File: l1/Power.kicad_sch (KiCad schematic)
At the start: 31 parts, among them IC1 LM2587S-ADJ, U1 TPS5430DDA, U2 TPS5430DDA

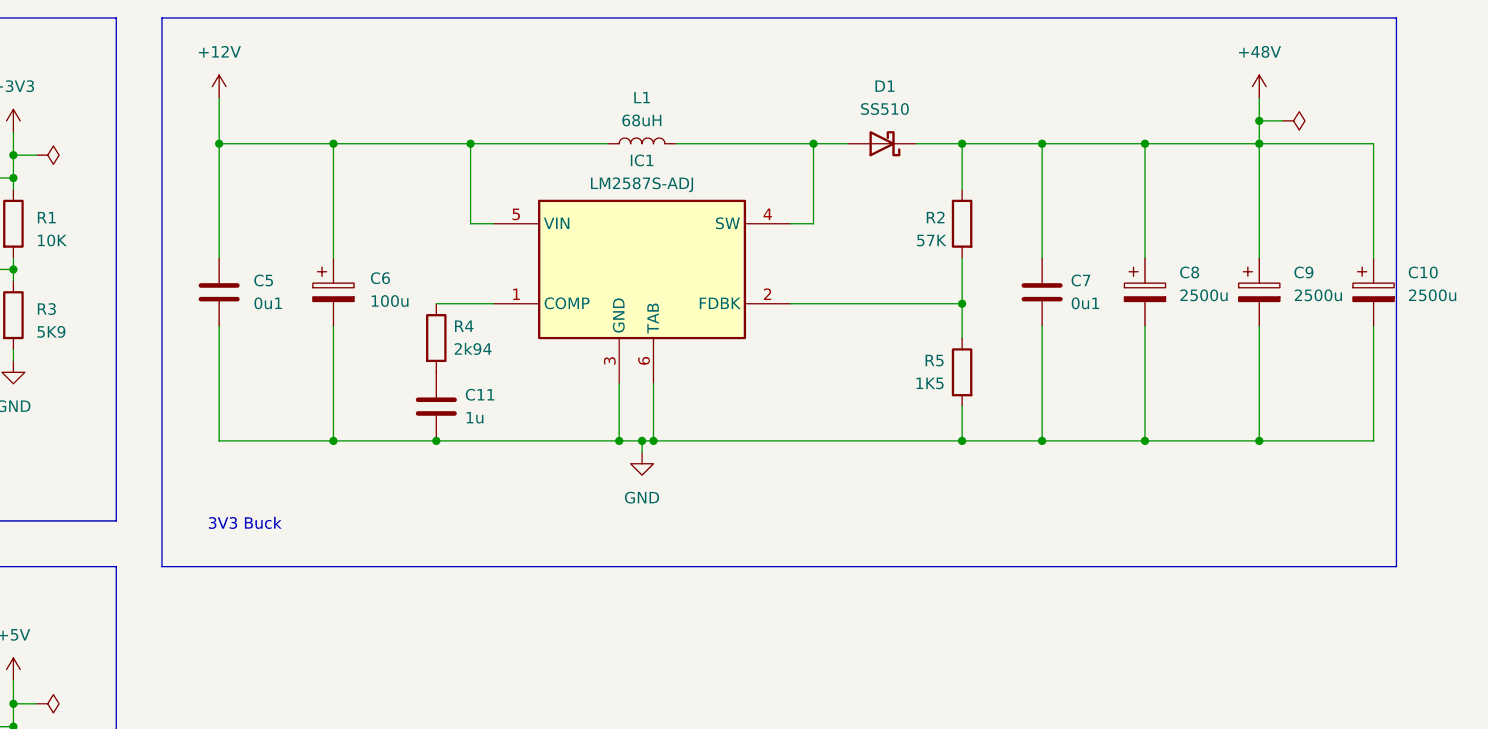
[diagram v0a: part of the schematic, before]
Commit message: Changed To G071
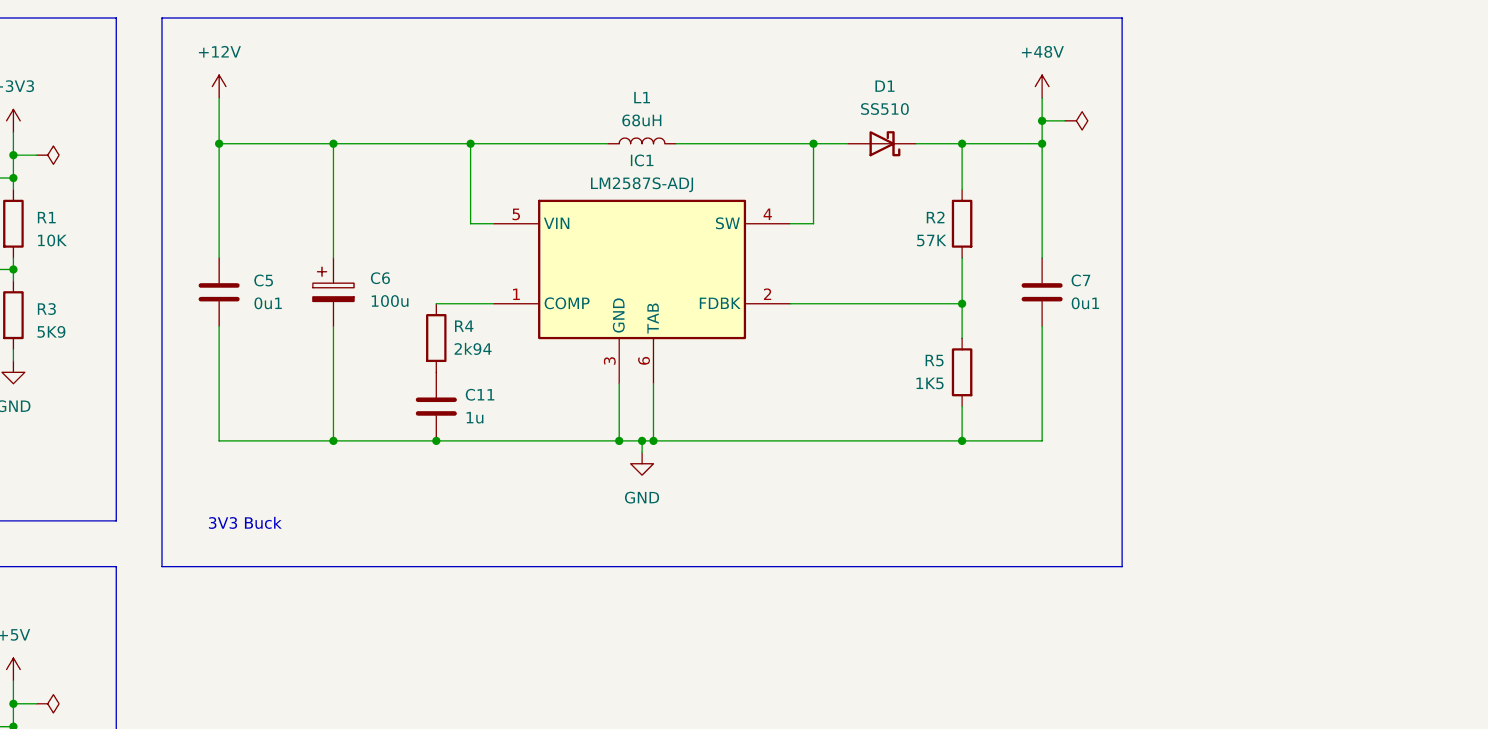
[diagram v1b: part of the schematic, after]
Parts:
- removed C10, C8, C9: 2500u, Library:CP_Radial_D16.0mm_P7.50mm, symbol Device:C_Polarized

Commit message: Changed To OKL
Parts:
- removed C1, C12: 10n, Library:cap0603, symbol Device:C
- removed C13, C2: 220u, Library:eia-7343-d, symbol Device:C_Polarized
- removed C14, C3: 0u1, Library:cap0603, symbol Device:C
- removed C15: 10u, Library:cap0603, symbol Device:C
- removed D2, D3: SS54, Library:SMA (DO-214AC), symbol Diode:B340
- removed L2, L3: 15uH, Library:0630 One Piece Inductor, symbol Device:L_Iron
- removed R1, R6: 10K, Library:res0603, symbol Device:R
- removed R3: 5K9, Library:res0603, symbol Device:R
- removed R7: 3K24, Library:res0603, symbol Device:R
- removed U1, U2: TPS5430DDA, Library:TI_SO-PowerPAD-8, symbol Regulator_Switching:TPS5430DDA
- added C? (x2): 10u, Library:cap0603, symbol Device:C
- added C?: 22u, Library:cap0603, symbol Device:C
- added R?: 2K18, symbol Device:R
- added R? (x2): 10K, symbol Device:R
- added R?: 1K34, symbol Device:R
- added U? (x2): OKL-T6-W12-C, symbol senrobo_kicad:OKL-T6-W12-C
- C4: value 10u -> 22u
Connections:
- net +12V: now also C?.1, R?.1, R?.1, U?.2 (VIN), U?.2 (VIN)
- net +3V3: now also C?.1, U?.4 (OUT), U?.5 (SENSE)
- net +5V: now also C?.1, U?.4 (OUT), U?.5 (SENSE)
- net GND: now also C?.2, C?.2, C?.2, R?.2, R?.2, U?.3 (GND), U?.3 (GND), U?.7 (GND), U?.7 (GND)
- new net: R?.1, U?.6 (TRIM) (x2)
- new net: R?.2, U?.1 (ON/OFF) (x2)
- new net: U?.10, U?.11, U?.9 (x2)
- no-connect marks 2 -> 0
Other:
- note added: "Boost"
- moved on the sheet: C11, C4, C5, C6, C7, D1, IC1, L1, R2, R4, R5

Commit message: Changed To OKL
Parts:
- added C? (x2): 220u, symbol Device:C_Polarized
- C?: value 10u -> 0u1
- R?: value 2K18 -> R
- R?: value 1K34 -> R
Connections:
- net +3V3: now also C?.1
- net +5V: now also C?.1
- net GND: now also C?.2, C?.2
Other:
- moved on the sheet: C?, R?, U?

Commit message: rough ideation
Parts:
- gave numbers to parts that had none: 11
- renumbered C11 to C10, C5 to C7, C6 to C8, C7 to C9, R2 to R5, R4 to R6, R5 to R7
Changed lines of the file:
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@@
 		(dnp no)
 		(fields_autoplaced yes)
-		(property "Reference" "R?"
+		(property "Reference" "R4"
 			(at 78.74 55.8799 0)
 			(effects
@@
 			(project ""
 				(path "/0e4ddce5-5c0a-41d1-ab67-e7bad6d98362/721a1ded-9f35-4b1d-b3f2-9ec7d8055788"
-					(reference "R?")
+					(reference "R4")
 					(unit 1)
 				)
@@
 		(on_board yes)
 		(dnp no)
-		(property "Reference" "R2"
+		(property "Reference" "R5"
 			(at 103.632 104.775 0)
 			(effects
@@
 			(project "l1"
 				(path "/0e4ddce5-5c0a-41d1-ab67-e7bad6d98362/721a1ded-9f35-4b1d-b3f2-9ec7d8055788"
-					(reference "R2")
+					(reference "R5")
 					(unit 1)
 				)
@@
 		(dnp no)
 		(fields_autoplaced yes)
-		(property "Reference" "#PWR015"
+		(property "Reference" "#PWR012"
 			(at 171.45 69.85 0)
 			(effects
@@
 			(project "l1"
 				(path "/0e4ddce5-5c0a-41d1-ab67-e7bad6d98362/721a1ded-9f35-4b1d-b3f2-9ec7d8055788"
-					(reference "#PWR015")
+					(reference "#PWR012")
 					(unit 1)
 				)
@@
 		(dnp no)
 		(fields_autoplaced yes)
-		(property "Reference" "R?"
+		(property "Reference" "R1"
 			(at 134.62 46.9899 0)
 			(effects
@@
 			(project "l1"
 				(path "/0e4ddce5-5c0a-41d1-ab67-e7bad6d98362/721a1ded-9f35-4b1d-b3f2-9ec7d8055788"
-					(reference "R?")
+					(reference "R1")
 					(unit 1)
 				)
@@
 		(dnp no)
 		(fields_autoplaced yes)
-		(property "Reference" "R4"
+		(property "Reference" "R6"
 			(at 48.895 116.8399 0)
 			(effects
@@
 			(project "l1"
 				(path "/0e4ddce5-5c0a-41d1-ab67-e7bad6d98362/721a1ded-9f35-4b1d-b3f2-9ec7d8055788"
-					(reference "R4")
+					(reference "R6")
 					(unit 1)
 				)
@@
 		(dnp no)
 		(fields_autoplaced yes)
-		(property "Reference" "#PWR010"
+		(property "Reference" "#PWR06"
 			(at 121.92 43.18 0)
 			(effects
@@
 			(project "l1"
 				(path "/0e4ddce5-5c0a-41d1-ab67-e7bad6d98362/721a1ded-9f35-4b1d-b3f2-9ec7d8055788"
-					(reference "#PWR010")
+					(reference "#PWR06")
 					(unit 1)
 				)
@@
 		(dnp no)
 		(fields_autoplaced yes)
-		(property "Reference" "C11"
+		(property "Reference" "C10"
 			(at 50.165 124.4599 0)
 			(effects
@@
 			(project "l1"
 				(path "/0e4ddce5-5c0a-41d1-ab67-e7bad6d98362/721a1ded-9f35-4b1d-b3f2-9ec7d8055788"
-					(reference "C11")
+					(reference "C10")
 					(unit 1)
 				)
@@
 		(dnp no)
 		(fields_autoplaced yes)
-		(property "Reference" "C5"
+		(property "Reference" "C7"
 			(at 26.67 111.76 0)
 			(effects
@@
 			(project "l1"
 				(path "/0e4ddce5-5c0a-41d1-ab67-e7bad6d98362/721a1ded-9f35-4b1d-b3f2-9ec7d8055788"
-					(reference "C5")
+					(reference "C7")
 					(unit 1)
 				)
@@
 		(dnp no)
 		(fields_autoplaced yes)
-		(property "Reference" "C7"
+		(property "Reference" "C9"
 			(at 117.475 111.7599 0)
 			(effects
@@
 			(project "l1"
 				(path "/0e4ddce5-5c0a-41d1-ab67-e7bad6d98362/721a1ded-9f35-4b1d-b3f2-9ec7d8055788"
-					(reference "C7")
+					(reference "C9")
 					(unit 1)
 				)
@@
 		(dnp no)
 		(fields_autoplaced yes)
-		(property "Reference" "R?"
+		(property "Reference" "R2"
 			(at 39.37 48.2599 0)
 			(effects
@@
 			(project ""
 				(path "/0e4ddce5-5c0a-41d1-ab67-e7bad6d98362/721a1ded-9f35-4b1d-b3f2-9ec7d8055788"
-					(reference "R?")
+					(reference "R2")
 					(unit 1)
 				)
@@
 		(dnp no)
 		(fields_autoplaced yes)
-		(property "Reference" "U?"
+		(property "Reference" "U2"
 			(at 53.34 35.56 0)
 			(effects
@@
 			(project ""
 				(path "/0e4ddce5-5c0a-41d1-ab67-e7bad6d98362/721a1ded-9f35-4b1d-b3f2-9ec7d8055788"
-					(reference "U?")
+					(reference "U2")
 					(unit 1)
 				)
@@
 		(dnp no)
 		(fields_autoplaced yes)
-		(property "Reference" "#PWR012"
+		(property "Reference" "#PWR013"
 			(at 76.2 71.12 0)
 			(effects
@@
 			(project "l1"
 				(path "/0e4ddce5-5c0a-41d1-ab67-e7bad6d98362/721a1ded-9f35-4b1d-b3f2-9ec7d8055788"
-					(reference "#PWR012")
+					(reference "#PWR013")
 					(unit 1)
 				)
@@
 		(dnp no)
 		(fields_autoplaced yes)
-		(property "Reference" "U?"
+		(property "Reference" "U1"
 			(at 148.59 34.29 0)
 			(effects
@@
 			(project "l1"
 				(path "/0e4ddce5-5c0a-41d1-ab67-e7bad6d98362/721a1ded-9f35-4b1d-b3f2-9ec7d8055788"
-					(reference "U?")
+					(reference "U1")
 					(unit 1)
 				)
@@
 		(dnp no)
 		(fields_autoplaced yes)
-		(property "Reference" "C?"
+		(property "Reference" "C6"
 			(at 100.33 51.1809 0)
 			(effects
@@
 			(project ""
 				(path "/0e4ddce5-5c0a-41d1-ab67-e7bad6d98362/721a1ded-9f35-4b1d-b3f2-9ec7d8055788"
-					(reference "C?")
+					(reference "C6")
 					(unit 1)
 				)
@@
 		(on_board yes)
 		(dnp no)
-		(property "Reference" "#PWR014"
+		(property "Reference" "#PWR010"
 			(at 121.92 68.58 0)
 			(effects
@@
 			(project "l1"
 				(path "/0e4ddce5-5c0a-41d1-ab67-e7bad6d98362/721a1ded-9f35-4b1d-b3f2-9ec7d8055788"
-					(reference "#PWR014")
+					(reference "#PWR010")
 					(unit 1)
 				)
@@
 		(on_board yes)
 		(dnp no)
-		(property "Reference" "C?"
+		(property "Reference" "C5"
 			(at 88.9 52.705 0)
 			(effects
@@
 			(project "l1"
 				(path "/0e4ddce5-5c0a-41d1-ab67-e7bad6d98362/721a1ded-9f35-4b1d-b3f2-9ec7d8055788"
-					(reference "C?")
+					(reference "C5")
 					(unit 1)
 				)
@@
 		(dnp no)
 		(fields_autoplaced yes)
-		(property "Reference" "#PWR06"
+		(property "Reference" "#PWR014"
 			(at 22.86 95.25 0)
 			(effects
@@
 			(project "l1"
 				(path "/0e4ddce5-5c0a-41d1-ab67-e7bad6d98362/721a1ded-9f35-4b1d-b3f2-9ec7d8055788"
-					(reference "#PWR06")
+					(reference "#PWR014")
 					(unit 1)
 				)
@@
 		(on_board yes)
 		(dnp no)
-		(property "Reference" "C?"
+		(property "Reference" "C2"
 			(at 184.15 51.435 0)
 			(effects
@@
 			(project "l1"
 				(path "/0e4ddce5-5c0a-41d1-ab67-e7bad6d98362/721a1ded-9f35-4b1d-b3f2-9ec7d8055788"
-					(reference "C?")
+					(reference "C2")
 					(unit 1)
 				)
@@
 		(dnp no)
 		(fields_autoplaced yes)
-		(property "Reference" "#PWR07"
+		(property "Reference" "#PWR015"
 			(at 114.3 95.25 0)
 			(effects
@@
 			(project "l1"
 				(path "/0e4ddce5-5c0a-41d1-ab67-e7bad6d98362/721a1ded-9f35-4b1d-b3f2-9ec7d8055788"
-					(reference "#PWR07")
+					(reference "#PWR015")
 					(unit 1)
 				)
@@
 		(dnp no)
 		(fields_autoplaced yes)
-		(property "Reference" "#FLG03"
+		(property "Reference" "#FLG05"
 			(at 118.745 93.98 0)
 			(effects
@@
 			(project "l1"
 				(path "/0e4ddce5-5c0a-41d1-ab67-e7bad6d98362/721a1ded-9f35-4b1d-b3f2-9ec7d8055788"
-					(reference "#FLG03")
+					(reference "#FLG05")
 					(unit 1)
 				)
@@
 		(on_board yes)
 		(dnp no)
-		(property "Reference" "C?"
+		(property "Reference" "C1"
 			(at 125.73 51.435 0)
 			(effects
@@
 			(project "l1"
 				(path "/0e4ddce5-5c0a-41d1-ab67-e7bad6d98362/721a1ded-9f35-4b1d-b3f2-9ec7d8055788"
-					(reference "C?")
+					(reference "C1")
 					(unit 1)
 				)
@@
 		(dnp no)
 		(fields_autoplaced yes)
-		(property "Reference" "C?"
+		(property "Reference" "C3"
 			(at 195.58 49.9109 0)
 			(effects
@@
 			(project "l1"
 				(path "/0e4ddce5-5c0a-41d1-ab67-e7bad6d98362/721a1ded-9f35-4b1d-b3f2-9ec7d8055788"
-					(reference "C?")
+					(reference "C3")
 					(unit 1)
 				)
@@
 		(on_board yes)
 		(dnp no)
-		(property "Reference" "#PWR013"
+		(property "Reference" "#PWR011"
 			(at 26.67 69.85 0)
 			(effects
@@
 			(project "l1"
 				(path "/0e4ddce5-5c0a-41d1-ab67-e7bad6d98362/721a1ded-9f35-4b1d-b3f2-9ec7d8055788"
-					(reference "#PWR013")
+					(reference "#PWR011")
 					(unit 1)
 				)
@@
 		(dnp no)
 		(fields_autoplaced yes)
-		(property "Reference" "R?"
+		(property "Reference" "R3"
 			(at 173.99 54.6099 0)
 			(effects
@@
 			(project "l1"
 				(path "/0e4ddce5-5c0a-41d1-ab67-e7bad6d98362/721a1ded-9f35-4b1d-b3f2-9ec7d8055788"
-					(reference "R?")
+					(reference "R3")
 					(unit 1)
 				)
@@
 		(dnp no)
 		(fields_autoplaced yes)
-		(property "Reference" "#FLG05"
+		(property "Reference" "#FLG03"
 			(at 198.755 41.91 0)
 			(effects
@@
 			(project "l1"
 				(path "/0e4ddce5-5c0a-41d1-ab67-e7bad6d98362/721a1ded-9f35-4b1d-b3f2-9ec7d8055788"
-					(reference "#FLG05")
+					(reference "#FLG03")
 					(unit 1)
 				)
@@
 		(on_board yes)
 		(dnp no)
-		(property "Reference" "C6"
+		(property "Reference" "C8"
 			(at 39.624 111.506 0)
 			(effects
@@
 			(project "l1"
 				(path "/0e4ddce5-5c0a-41d1-ab67-e7bad6d98362/721a1ded-9f35-4b1d-b3f2-9ec7d8055788"
-					(reference "C6")
+					(reference "C8")
 					(unit 1)
 				)
@@
 		(on_board yes)
 		(dnp no)
-		(property "Reference" "R5"
+		(property "Reference" "R7"
 			(at 103.505 120.6499 0)
 			(effects
@@
 			(project "l1"
 				(path "/0e4ddce5-5c0a-41d1-ab67-e7bad6d98362/721a1ded-9f35-4b1d-b3f2-9ec7d8055788"
-					(reference "R5")
+					(reference "R7")
 					(unit 1)
 				)
@@
 		(dnp no)
 		(fields_autoplaced yes)
-		(property "Reference" "#PWR011"
+		(property "Reference" "#PWR07"
 			(at 191.77 43.18 0)
 			(effects
@@
 			(project ""
 				(path "/0e4ddce5-5c0a-41d1-ab67-e7bad6d98362/721a1ded-9f35-4b1d-b3f2-9ec7d8055788"
-					(reference "#PWR011")
-					(unit 1)
-				)
+					(reference "#PWR07")
+					(unit 1)
+				)
